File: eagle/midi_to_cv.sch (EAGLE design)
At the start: 30 parts, among them IC1 TL074P, IC4 TL074P, IC5 TL074P, U1 ATMEGA328P_PDIP

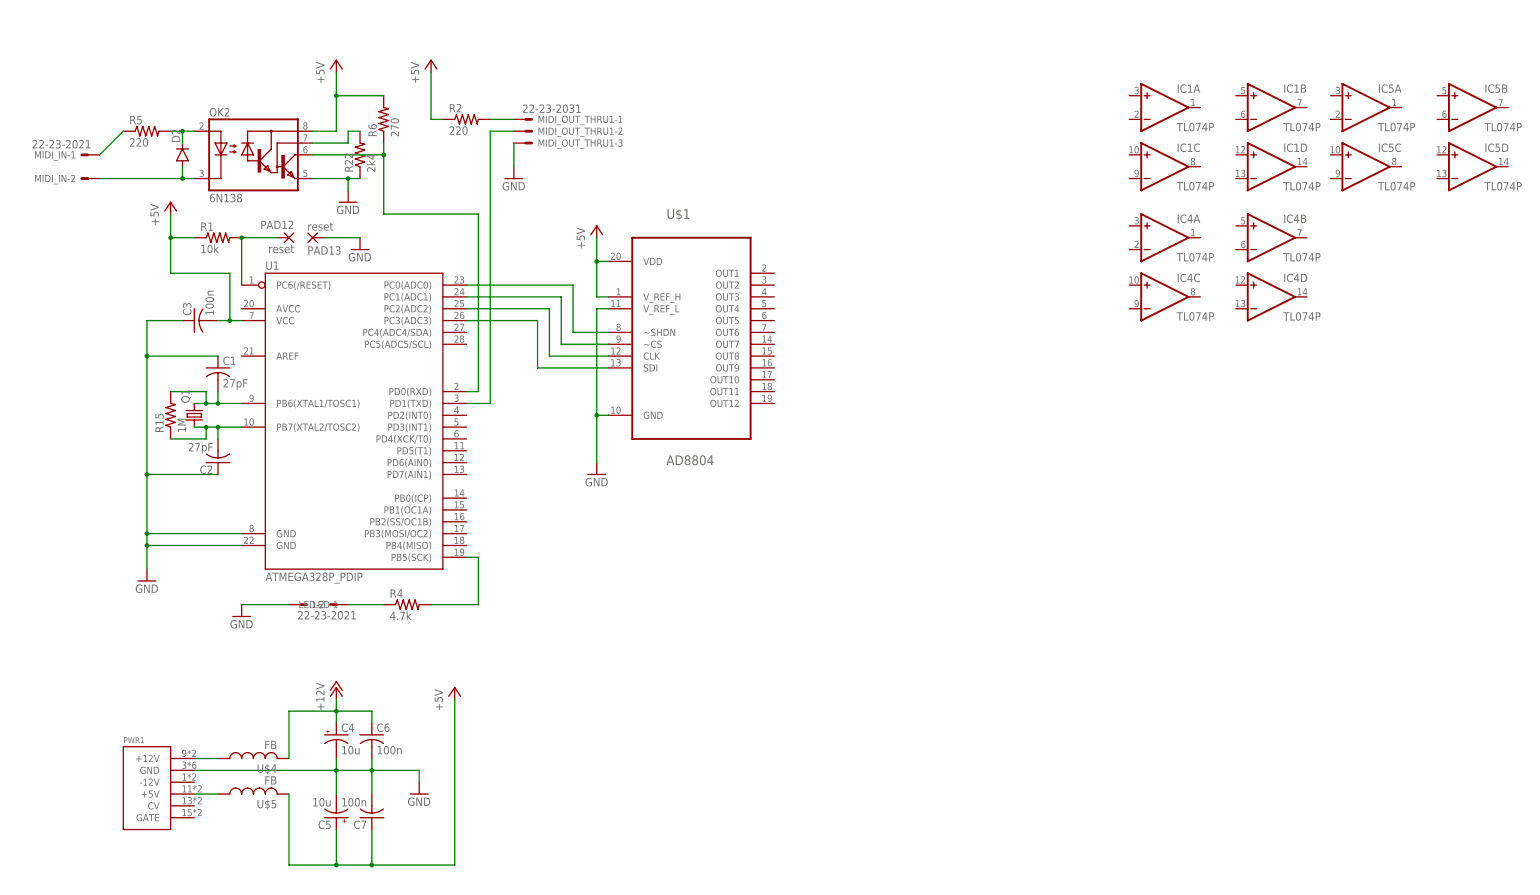
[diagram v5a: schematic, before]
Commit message: first opamps
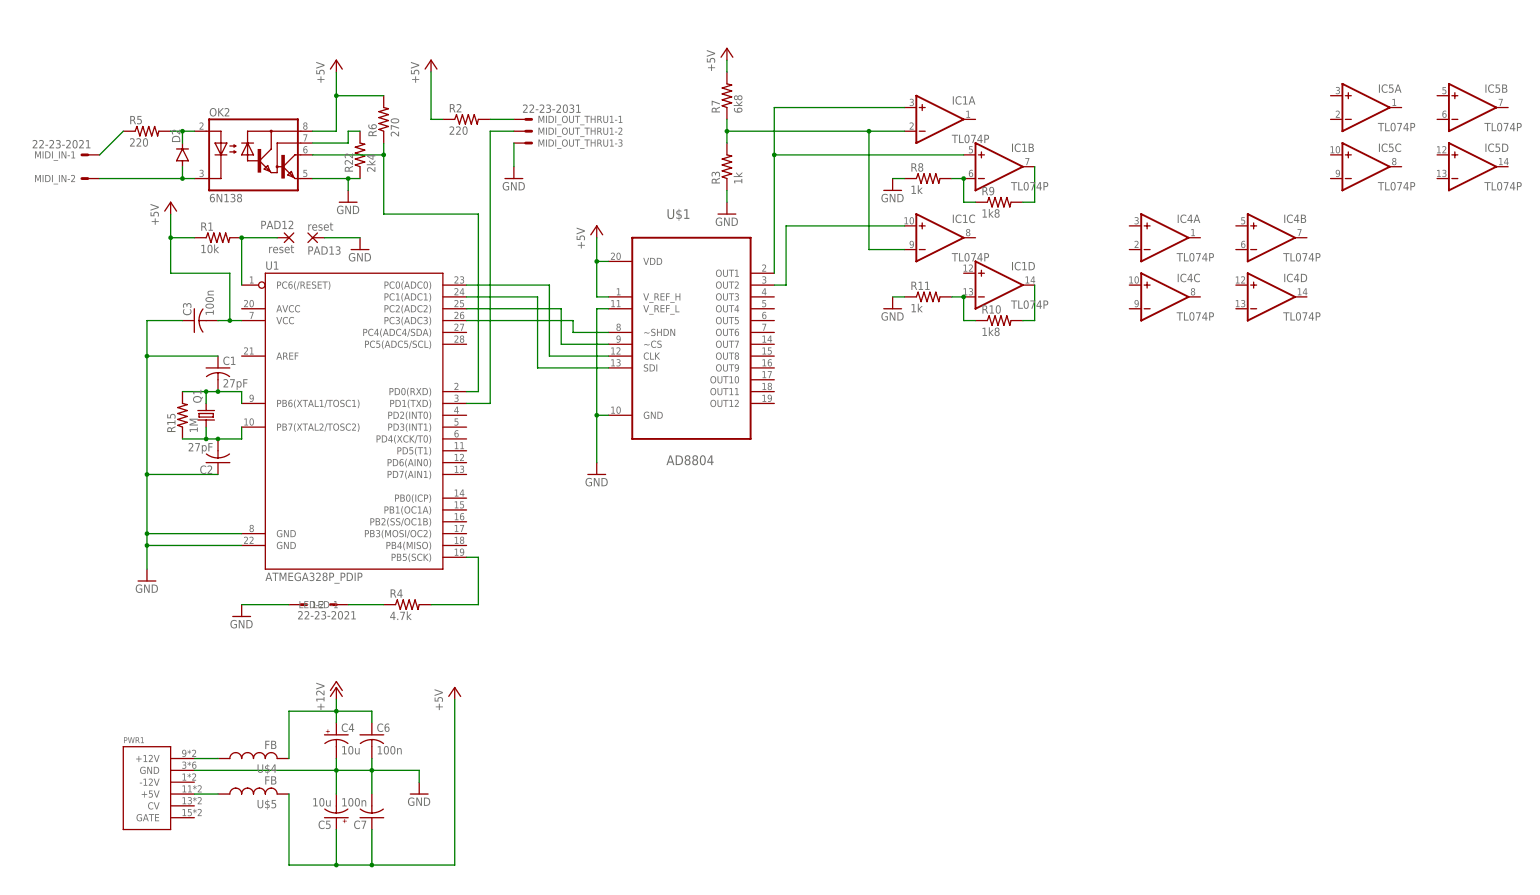
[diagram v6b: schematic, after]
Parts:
- added R10, R9: 1k8, rcl:R-US_0207/10
- added R11, R3, R8: 1k, rcl:R-US_0207/10
- added R7: 6k8, rcl:R-US_0207/10
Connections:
- new net N$13: IC1A.-IN, IC1C.-IN, R3.2, R7.1
- new net N$14: IC1A.+IN, IC1B.+IN, U$1.OUT1
- new net N$15: IC1B.-IN, R8.2, R9.1
- new net N$16: IC1B.OUT, R9.2
- new net N$21: IC1D.-IN, R10.1, R11.2
- new net N$22: IC1C.+IN, U$1.OUT2
- new net N$23: IC1D.OUT, R10.2
- net +5V: now also R7.2
- net GND: now also R11.1, R3.1, R8.1
- net N$3: now also U1.PC3(ADC3); no longer U1.PC0(ADC0)
- net N$6: now also U1.PC2(ADC2); no longer U1.PC1(ADC1)
- net N$7: now also U1.PC0(ADC0); no longer U1.PC2(ADC2)
- net N$8: now also U1.PC1(ADC1); no longer U1.PC3(ADC3)
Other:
- moved on the sheet: IC1A, IC1B, IC1C, IC1D, Q1, R15

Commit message: routed
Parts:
- added C10, C12, C8: 100n, rcl:C-US025-024X044
- added R12, R20, R29, R32, R34, R35, R36, R37, R38, R39, R40, R41, R43: 1k, rcl:R-US_0204/7
- added R13, R14, R16, R19, R21, R23, R28, R30, R31, R33, R42: 1k, rcl:R-US_0204/5
- added R17, R18, R24, R25, R26, R27: 1k8, rcl:R-US_0204/2V
- added X1, X2: (no value), con-molex:KK-156-6
- R10, R9: device rcl:R-US_0207/10 -> rcl:R-US_0204/2V
- R11, R3, R8: value 1k -> 1k8; device rcl:R-US_0207/10 -> rcl:R-US_0204/2V
- R5: device rcl:R-US_0207/10 -> rcl:R-US_0204/7
- R7: value 6k8 -> 1k8; device rcl:R-US_0207/10 -> rcl:R-US_0204/2V
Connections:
- new net N$24: IC4C.-IN, R17.1, R19.2
- new net N$25: R34.2, X1-1.S
- new net N$26: IC1A.+IN, U$1.OUT1
- new net N$27: IC1B.+IN, U$1.OUT2
- new net N$28: IC1C.+IN, U$1.OUT3
- new net N$29: IC1D.+IN, U$1.OUT4
- new net N$30: IC4B.-IN, R20.2, R7.1
- new net N$31: IC4A.-IN, R21.2, R3.1
- new net N$32: IC4B.+IN, U$1.OUT5
- new net N$33: IC4A.+IN, U$1.OUT6
- new net N$34: IC4D.+IN, U$1.OUT7
- new net N$35: IC4C.+IN, U$1.OUT8
- new net N$36: IC4D.-IN, R18.1, R23.2
- new net N$37: IC4A.OUT, R3.2, R37.1
- new net N$38: R35.2, X1-2.S
- new net N$39: R33.2, X1-3.S
- new net N$40: R32.2, X1-4.S
- new net N$41: IC5A.+IN, U$1.OUT9
- new net N$42: IC5B.+IN, U$1.OUT10
- new net N$43: IC5C.+IN, U$1.OUT11
- new net N$44: IC5D.+IN, U$1.OUT12
- new net N$45: IC5A.-IN, R24.1, R28.2
- new net N$46: IC5B.-IN, R25.1, R29.2
- new net N$47: IC5C.-IN, R26.1, R30.2
- new net N$48: IC5D.-IN, R27.1, R31.2
- new net N$49: IC5A.OUT, R24.2, R40.1
- new net N$50: IC5B.OUT, R25.2, R41.1
- new net N$51: IC5C.OUT, R26.2, R42.1
- new net N$52: IC5D.OUT, R27.2, R43.1
- new net N$53: IC1A.OUT, R32.1, R8.2
- new net N$54: IC1B.OUT, R33.1, R9.2
- new net N$55: IC1C.OUT, R10.2, R34.1
- new net N$56: IC1D.OUT, R11.2, R35.1
- new net N$57: R36.2, X1-5.S
- new net N$58: R37.2, X1-6.S
- new net N$59: R40.2, X2-1.S
- new net N$61: R41.2, X2-2.S
- new net N$63: R42.2, X2-3.S
- new net N$64: R43.2, X2-4.S
- new net N$65: R39.2, X2-5.S
- new net N$66: R38.2, X2-6.S
- net +12V: now also C10.1, C12.1, C8.1, IC1P.V+, IC4P.V+, IC5P.V+
- net +5V: no longer R7.2
- net GND: now also C10.2, C12.2, C8.2, IC1P.V-, IC4P.V-, IC5P.V-, R12.1, R13.1, R14.1, R16.1, R19.1, R20.1, R21.1, R23.1, R28.1, R29.1, R30.1, R31.1; no longer R11.1, R3.1, R8.1
- net N$13: now also R12.2, R8.1; no longer IC1C.-IN, R3.2, R7.1
- net N$14: now also IC1C.-IN, R10.1, R14.2; no longer IC1A.+IN, IC1B.+IN, U$1.OUT1
- net N$15: now also R13.2; no longer R8.2
- net N$16: now also IC4B.OUT, R36.1, R7.2; no longer IC1B.OUT, R9.2
- net N$21: now also R11.1, R16.2; no longer R10.1, R11.2
- net N$22: now also IC4C.OUT, R17.2, R39.1; no longer IC1C.+IN, U$1.OUT2
- net N$23: now also IC4D.OUT, R18.2, R38.1; no longer IC1D.OUT, R10.2
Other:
- moved on the sheet: IC1A, IC1B, IC1C, IC1D, IC4A, IC4B, IC4C, IC4D, IC5A, IC5B, IC5C, IC5D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

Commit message: tweaks
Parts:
- R29, R35, R41: device rcl:R-US_0204/7 -> rcl:R-US_0204/5
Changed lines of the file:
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@@
 <part name="R27" library="rcl" deviceset="R-US_" device="0204/2V" value="1k8"/>
 <part name="R28" library="rcl" deviceset="R-US_" device="0204/5" value="1k"/>
-<part name="R29" library="rcl" deviceset="R-US_" device="0204/7" value="1k"/>
+<part name="R29" library="rcl" deviceset="R-US_" device="0204/5" value="1k"/>
 <part name="R30" library="rcl" deviceset="R-US_" device="0204/5" value="1k"/>
 <part name="R31" library="rcl" deviceset="R-US_" device="0204/5" value="1k"/>
@@
 <part name="R33" library="rcl" deviceset="R-US_" device="0204/5" value="1k"/>
 <part name="R34" library="rcl" deviceset="R-US_" device="0204/7" value="1k"/>
-<part name="R35" library="rcl" deviceset="R-US_" device="0204/7" value="1k"/>
+<part name="R35" library="rcl" deviceset="R-US_" device="0204/5" value="1k"/>
 <part name="R36" library="rcl" deviceset="R-US_" device="0204/7" value="1k"/>
 <part name="R37" library="rcl" deviceset="R-US_" device="0204/7" value="1k"/>
@@
 <part name="R39" library="rcl" deviceset="R-US_" device="0204/7" value="1k"/>
 <part name="R40" library="rcl" deviceset="R-US_" device="0204/7" value="1k"/>
-<part name="R41" library="rcl" deviceset="R-US_" device="0204/7" value="1k"/>
+<part name="R41" library="rcl" deviceset="R-US_" device="0204/5" value="1k"/>
 <part name="R42" library="rcl" deviceset="R-US_" device="0204/5" value="1k"/>
 <part name="R43" library="rcl" deviceset="R-US_" device="0204/7" value="1k"/>
